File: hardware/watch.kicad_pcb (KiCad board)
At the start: 2 copper layers, 24 x 24 mm, 30 parts, among them J1 DEBUG, J2 RTC_CALIB, J3 RST, Q1 BC846, SW1 MODE, SW2 ALARM, SW3 LIGHT, U1 STM32L053C8Ux, U2 LCD, Y1 32.768kHz

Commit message: Use Paw Connect for debug connector
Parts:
- removed J3: RST, TestPoint:TestPoint_Pad_1.0x1.0mm
- J1: value DEBUG -> Debug; footprint Jumper:SolderJumper-2_P1.3mm_Open_Pad1.0x1.5mm -> Paw-Connect:Paw-Connect_RevB_TC2030-IDC-NL_2x03_P1.27mm_Vertical; moved to B.Cu
- moved J1 8.60 mm to (160.2, 78.8), turned to -152.5 degrees
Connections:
- J1 pad 1: /SWDIO -> VCC
- J1 pad 2: /SWCLK -> /SWDIO
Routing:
- net /SWDIO: track 3.42 -> 11.9 mm, vias 0 -> 1
- net /SWCLK: track 4.23 -> 11.7 mm, vias 0 -> 1
- net /LCD_SEG2: track 10.8 -> 7.83 mm
- net GND: track 28.5 -> 31.4 mm
- net /LCD_SEG1: track 11.2 -> 8.58 mm
- net /LCD_SEG0: track 12.6 -> 10.7 mm
- net /NRST: track 5.41 -> 3.65 mm
- net /LCD_SEG4: track 8.05 -> 6.34 mm
- net /LCD_SEG3: track 8.28 -> 7.09 mm
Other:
- board text added: "CR2016"
- board text removed: "3v"
- board text removed: "C D"
- board text removed: "C: SWCLK D: SWDIO"
- board text removed: "~{RST}"

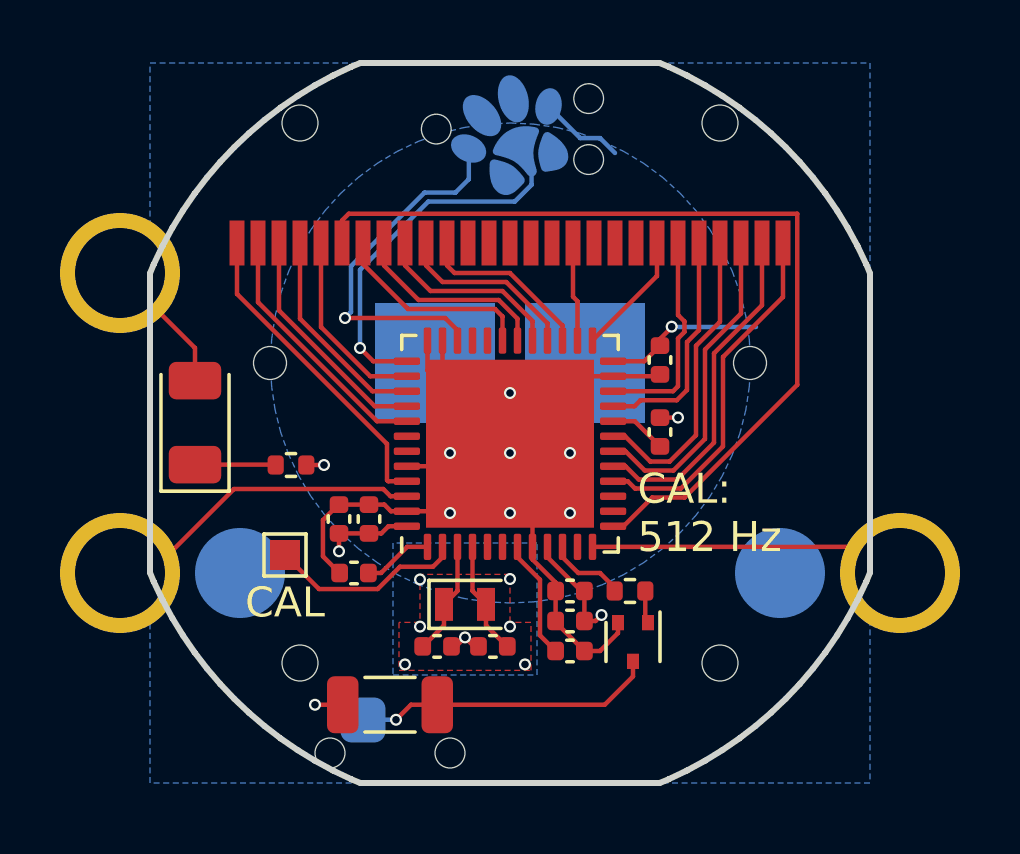
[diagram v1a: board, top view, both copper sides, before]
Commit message: Move to MSP430FR6972 based hardware
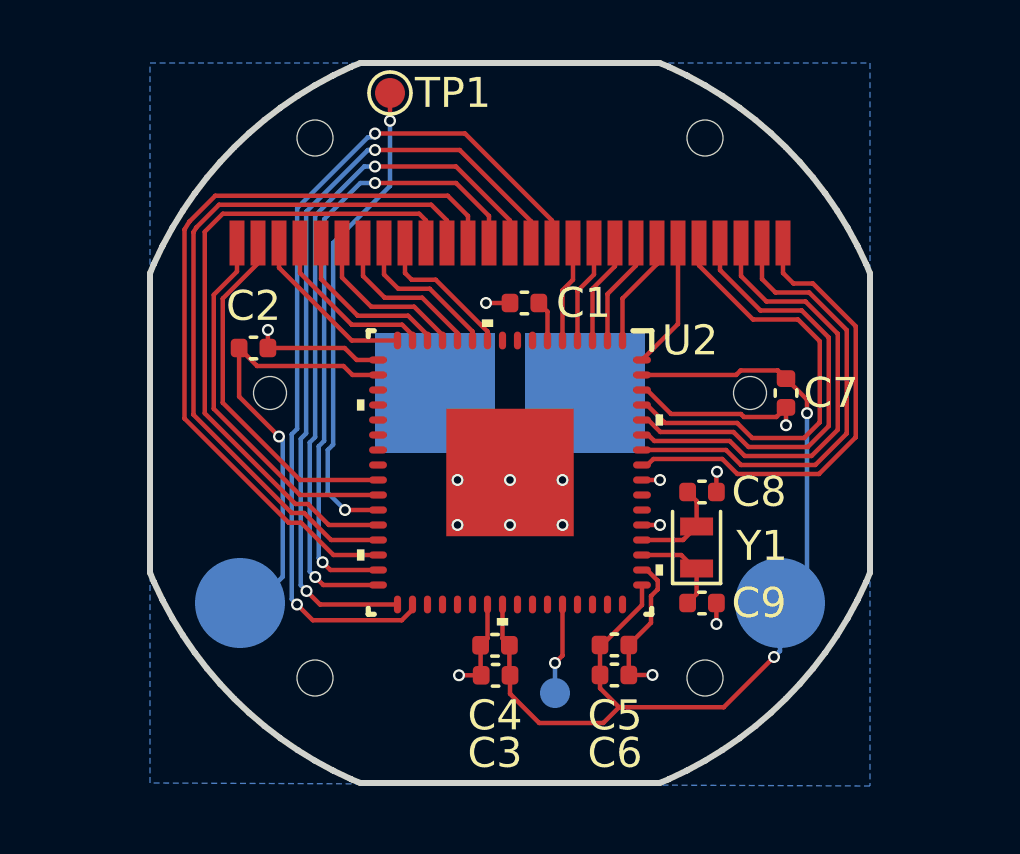
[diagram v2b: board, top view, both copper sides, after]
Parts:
- removed C10: 100n, Capacitor_SMD:C_0402_1005Metric
- removed C11: 1u, Capacitor_SMD:C_0402_1005Metric
- removed D1: LED, LED_SMD:LED_1206_3216Metric
- removed J1: Debug, Paw-Connect:Paw-Connect_RevB_TC2030-IDC-NL_2x03_P1.27mm_Vertical
- removed J2: RTC_CALIB, TestPoint:TestPoint_Pad_1.0x1.0mm
- removed L1: L, Inductor_SMD:L_1206_3216Metric
- removed LS1: Piezo, f-91w:Buzzer
- removed Q1: BC846, Package_TO_SOT_SMD:SOT-523
- removed R1: 460, Resistor_SMD:R_0402_1005Metric
- removed R3: 200R, Resistor_SMD:R_0402_1005Metric
- removed SW1: MODE, Watch:Button
- removed SW2: ALARM, Watch:Button
- removed SW3: LIGHT, Watch:Button
- removed the U1 at (159.8, 89.0)
- added C6: 1u, Capacitor_SMD:C_0402_1005Metric, F.Cu at (163.2, 96.7)
- added TP1: RX, TestPoint:TestPoint_Pad_D1.0mm, F.Cu at (155.8, 77.3)
- added TP2: RTCCLK, TestPoint:TestPoint_Pad_D1.0mm, B.Cu at (161.2, 97.3)
- added U2: MSP430FR6972IRGCR, MSP430FR6972:RGC0064B_NV, F.Cu at (159.8, 90.0)
- C1: value 100n -> 4u7
- C2: value 1u -> 100n
- C3: value 20p -> 1u
- C4: value 20p -> 100n
- C7: value 10u -> 100n
- C8, C9: value 100n -> 20p
- moved C7 15.5 mm to (168.9, 87.3), turned to -90 degrees
- moved C1 11.7 mm to (160.2, 84.3), turned to 180 degrees
- moved C9 11.4 mm to (166.2, 94.3), turned to 0 degrees
- moved C2 8.21 mm to (151.2, 85.8), turned to 0 degrees
- moved Y1 7.95 mm to (166.0, 92.5), turned to 90 degrees
- moved C5 7.26 mm to (163.2, 95.7), turned to 0 degrees
- moved C8 4.62 mm to (166.2, 90.6), turned to 0 degrees
- moved C3 2.17 mm to (159.3, 96.7), turned to 180 degrees
- moved BT1 1.00 mm to (159.8, 87.3)
- moved H1 0.71 mm to (153.2, 78.8)
- moved H2 0.71 mm to (153.2, 96.8)
- moved H3 0.71 mm to (166.2, 78.8)
- moved H4 0.71 mm to (166.2, 96.8)
- moved C4 0.08 mm to (159.3, 95.7)
- renumbered H4 to H1, H1 to H3, H3 to H4, U2 to U1
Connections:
- C1 pad 1: /NRST -> Net-(U2A-R33_LCDCAP)
- C2 pad 1: Net-(U1-VLCD) -> VCC
- C3 pad 1: /OSC32_IN -> VCC
- C4 pad 1: /OSC32_OUT -> VCC
- C5 pad 1: /LCD_VLCD2 -> VCC
- C8 pad 1: VCC -> Net-(U2A-PJ.5_LFXOUT)
- C9 pad 1: VCC -> Net-(U2A-PJ.4_LFXIN)
- U1 pad 12: unconnected-(U2-S8-Pad12) -> /LCD_SEG8
- U1 pad 13: unconnected-(U2-S9-Pad13) -> /LCD_SEG9
- U1 pad 14: unconnected-(U2-S10-Pad14) -> /LCD_SEG10
- U1 pad 15: unconnected-(U2-S11-Pad15) -> /LCD_SEG11
- U1 pad 16: unconnected-(U2-S12-Pad16) -> /LCD_SEG12
- U1 pad 17: /LCD_SEG8 -> /LCD_SEG13
- U1 pad 18: unconnected-(U2-S14-Pad18) -> /LCD_SEG14
- U1 pad 19: unconnected-(U2-S15-Pad19) -> /LCD_SEG15
- U1 pad 20: unconnected-(U2-S16-Pad20) -> /LCD_SEG16
- U1 pad 21: /LCD_SEG9 -> /LCD_SEG17
- U1 pad 22: /LCD_SEG10 -> /LCD_SEG18
- U1 pad 23: /LCD_SEG11 -> /LCD_SEG19
- U1 pad 24: /LCD_SEG12 -> /LCD_SEG20
- U1 pad 25: /LCD_SEG13 -> /LCD_SEG21
- U1 pad 26: /LCD_SEG14 -> /LCD_SEG22
- U1 pad 27: /LCD_SEG15 -> /LCD_SEG23
- Y1 pad 1: /OSC32_IN -> Net-(U2A-PJ.4_LFXIN)
- Y1 pad 2: /OSC32_OUT -> Net-(U2A-PJ.5_LFXOUT)
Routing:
- net VCC: track 12.5 -> 47.0 mm, vias 4 -> 3
- net /LCD_SEG5: track 29.5 -> 5.30 mm
- net /LCD_SEG8: track 3.62 -> 25.8 mm
- net /LCD_SEG12: track 10.2 -> 29.1 mm, vias 0 -> 2
- net /LCD_SEG11: track 7.75 -> 26.1 mm, vias 0 -> 2
- net /LCD_SEG7: track 5.59 -> 23.8 mm
- net /LCD_SEG9: track 4.14 -> 20.9 mm, vias 0 -> 2
- net Net-(U2A-P3.5_UCA1SOMI_UCA1RXD_TB0.1_S22): track 0.00 -> 16.1 mm, vias 0 -> 2
- net /LCD_SEG6: track 5.83 -> 21.8 mm
- net /LCD_SEG10: track 7.18 -> 23.1 mm, vias 0 -> 2
- net /LCD_SEG22: track 0.00 -> 15.6 mm
- net /LCD_SEG23: track 0.00 -> 15.6 mm
- net /LCD_SEG21: track 0.00 -> 15.3 mm
- net /LCD_SEG20: track 0.00 -> 15.1 mm
- net /LCD_SEG19: track 0.00 -> 15.0 mm
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- removed copper zone on F.Cu, net GND
- removed copper zone on B.Cu, net VCC
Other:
- board text added: "512Hz"
- board text removed: "CAL"
- board text removed: "CAL: 512 Hz"
- board text removed: "github/hugglesfox"
